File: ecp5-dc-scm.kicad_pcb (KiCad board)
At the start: 6 copper layers, 90 x 120.4 mm, 238 parts, among them IC1 TPS54561, J1 WE-RJ45_7499111121A, J10 61300611121, J11 S2B-PH-K-S_LF__SN_, J2 1-2199230-6, J3 543630489, J4 M20-7830642, J5 SFF-TA-1002-4C+, J6 2X05, Q1 IRLML6402TRPBF, Q10 2N7002, Q11 2N7002, Q12 2N7002, Q2 IRLML6402TRPBF, Q3 IRLML6402TRPBF, Q4 IRLML6402TRPBF, Q5 IRLML6402TRPBF, Q6 2N7002, Q7 2N7002, Q8 2N7002, Q9 2N7002, U1 KSZ9031RNXCA, U10 LM21212-2, U11 SN74LVC1G11DBVR, U14 TPS62823DLCT, U15 TPS62823DLCT, U16 TPS62823DLCT, U17 TPS62823DLCT, U18 ECP5UM5G_85_CABGA756, U2 W25Q32JVSSIQ_TR, U3 W25Q32JVSSIQ_TR, U4 W25Q32JVSSIQ_TR, U5 W25Q32JVSSIQ_TR, U6 NVT2008DQ,115, U7 AS4C256M16D3, U8 TPS51200DRC, Y1 ABM8G-25.000MHZ-18-D2Y-T

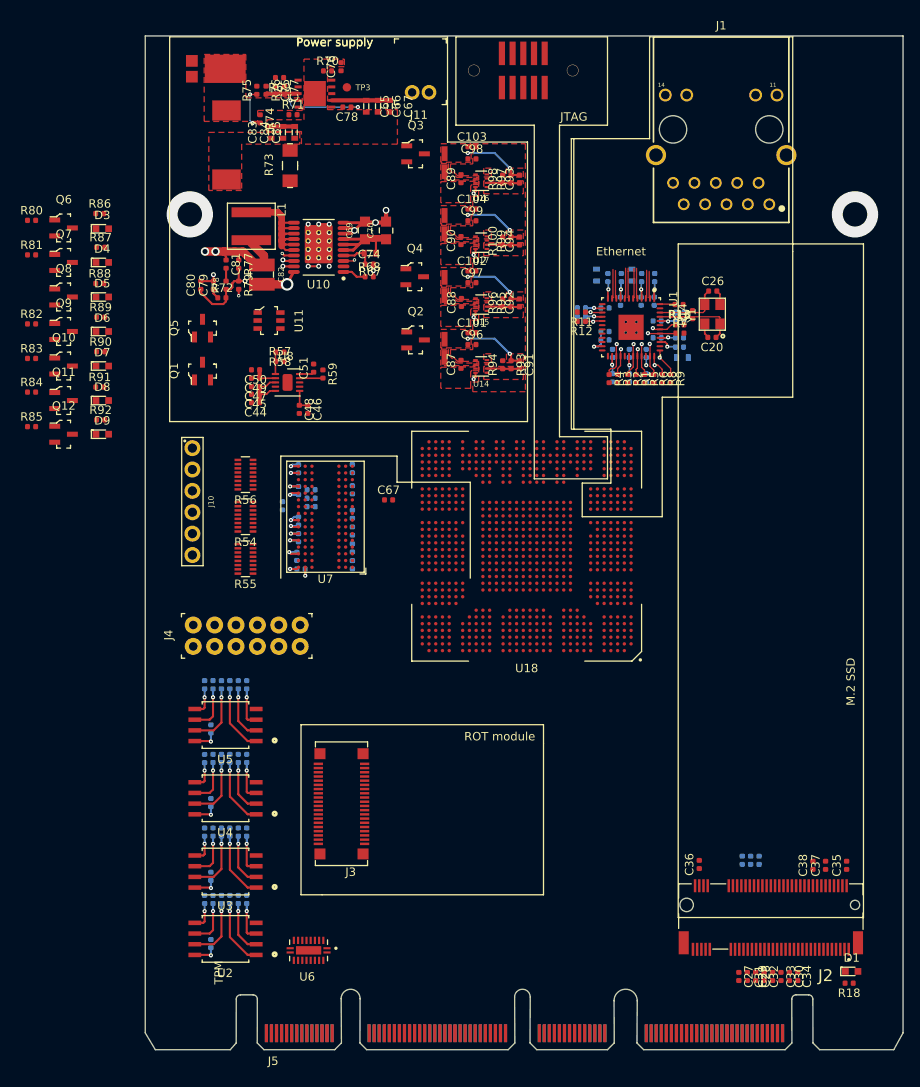
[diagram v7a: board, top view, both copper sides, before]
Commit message: Add component placement-power supply
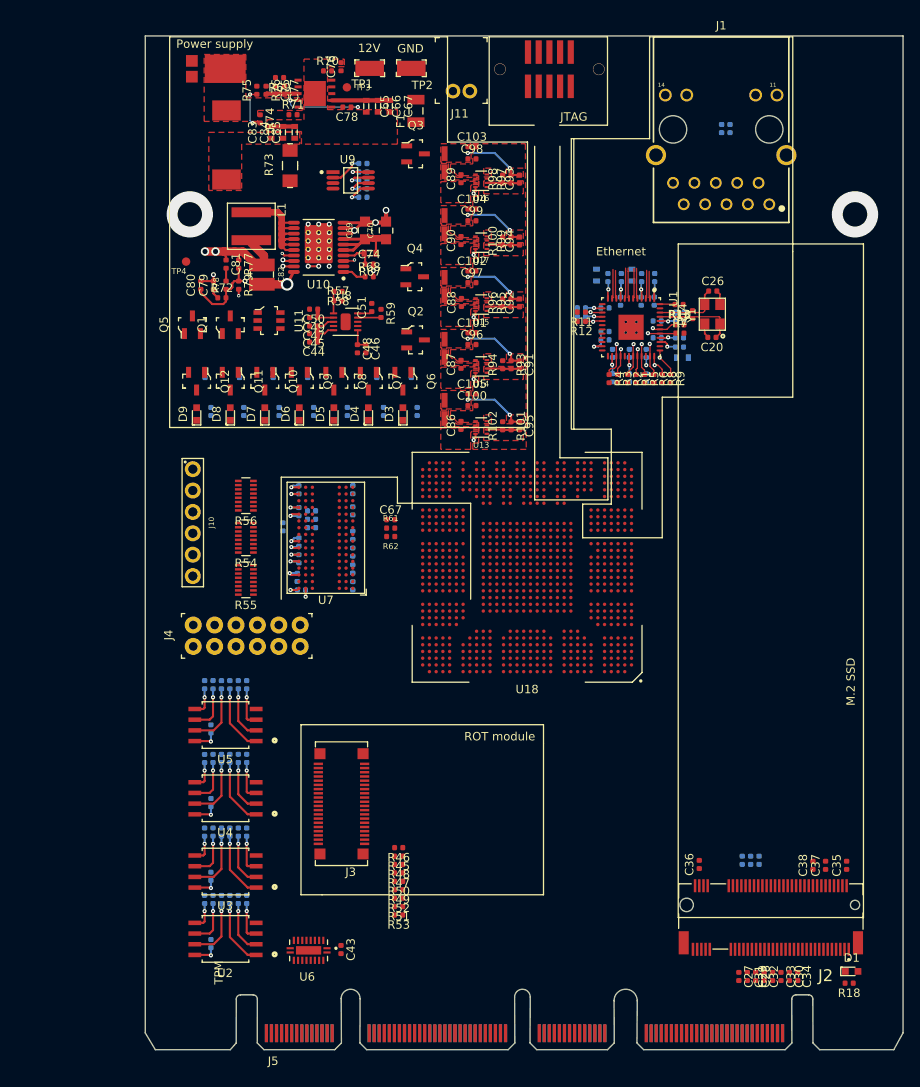
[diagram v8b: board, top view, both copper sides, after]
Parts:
- added C100: C_10u_0402, ecp5-dc-scm-footprints:0402-cap, F.Cu at (98.9, 102.8)
- added C105: C_10u_0402, ecp5-dc-scm-footprints:0402-cap, F.Cu at (98.9, 101.4)
- added C43: C_100n_0402, ecp5-dc-scm-footprints:0402-cap, F.Cu at (83.3, 167.4)
- added C68: C_10n_0402, ecp5-dc-scm-footprints:0402-cap, B.Cu at (86.0, 78.0)
- added C86: C_10u_0402, ecp5-dc-scm-footprints:0402-cap, F.Cu at (97.6, 105.2)
- added C95: C_120p_0402, ecp5-dc-scm-footprints:0402-res, F.Cu at (104.5, 105.2)
- added F1: 0466003.NR, antmicro-footprints:1206-Fuse-Littelfuse-0466-0-0-MFG, F.Cu at (92.2, 67.8)
- added L7: IHLP1212AEERR47M11, antmicro-footprints:IHLP-1212AE, F.Cu at (95.7, 103.2)
- added R101: R_453k_0402, ecp5-dc-scm-footprints:0402-res, F.Cu at (103.5, 105.2)
- added R102: R_100k_0402, ecp5-dc-scm-footprints:0402-res, F.Cu at (102.5, 105.2)
- added R15: R_1k_0402, ecp5-dc-scm-footprints:0402-res, B.Cu at (129.6, 69.9)
- added R16: R_1k_0402, ecp5-dc-scm-footprints:0402-res, B.Cu at (128.6, 69.9)
- added R45: R_357k_0402, ecp5-dc-scm-footprints:0402-res, F.Cu at (90.2, 156.3)
- added R46: R_357k_0402, ecp5-dc-scm-footprints:0402-res, F.Cu at (90.2, 155.3)
- added R47: R_357k_0402, ecp5-dc-scm-footprints:0402-res, F.Cu at (90.2, 158.3)
- added R48: R_357k_0402, ecp5-dc-scm-footprints:0402-res, F.Cu at (90.2, 157.3)
- added R49: R_357k_0402, ecp5-dc-scm-footprints:0402-res, F.Cu at (90.2, 160.3)
- added R50: R_357k_0402, ecp5-dc-scm-footprints:0402-res, F.Cu at (90.2, 159.3)
- added R51: R_357k_0402, ecp5-dc-scm-footprints:0402-res, F.Cu at (90.2, 162.3)
- added R52: R_357k_0402, ecp5-dc-scm-footprints:0402-res, F.Cu at (90.2, 161.3)
- added R53: R_200k_0402, ecp5-dc-scm-footprints:0402-res, F.Cu at (90.2, 163.3)
- added R61: R_51R_0402, antmicro-footprints:0402-res, F.Cu at (89.2, 117.3)
- added R62: R_51R_0402, antmicro-footprints:0402-res, F.Cu at (89.2, 118.3)
- added R63: R_1k1_0402, antmicro-footprints:0402-res, B.Cu at (86.0, 74.0)
- added R64: R_1k_0402, ecp5-dc-scm-footprints:0402-res, B.Cu at (86.0, 75.0)
- added R65: R_1k_0402, ecp5-dc-scm-footprints:0402-res, B.Cu at (86.0, 76.0)
- added R66: R_1k_0402, ecp5-dc-scm-footprints:0402-res, B.Cu at (86.0, 77.0)
- added TP1: RCW-0C, antmicro-footprints:PROBE_PAD_1206, F.Cu at (86.8, 62.8)
- added TP2: RCW-0C, antmicro-footprints:PROBE_PAD_1206, F.Cu at (91.7, 62.8)
- added TP4: TP_SMD1MM, ecp5-dc-scm-footprints:Testpoint_smd_1mm, F.Cu at (65.0, 85.8)
- added U13: TPS62823DLCT, ecp5-dc-scm-footprints:QFN-8_2x1mm, F.Cu at (100.0, 105.4)
- added U9: LM3881MME_NOPB, ecp5-dc-scm-footprints:VSSOP8-Texas_Instruments-DGK0008A, F.Cu at (84.5, 76.0)
- R80, R81, R82, R83, R84, R85, R86, R87, R88, R89, R90, R91, R92: moved to B.Cu
- moved R80 48.6 mm to (91.7, 99.0), turned to 90 degrees
- moved R86 44.4 mm to (92.4, 103.5), turned to 90 degrees
- moved Q6 44.2 mm to (90.7, 99.9), turned to 270 degrees
- moved R81 43.4 mm to (87.6, 99.0), turned to 90 degrees
- moved D3 41.9 mm to (90.7, 103.8), turned to 90 degrees
- moved Q7 38.8 mm to (86.6, 99.9), turned to 270 degrees
- moved R87 38.8 mm to (88.4, 103.5), turned to 90 degrees
- moved D4 36.4 mm to (86.6, 103.8), turned to 90 degrees
- moved Q8 33.6 mm to (82.5, 99.9), turned to 270 degrees
- moved R82 33.3 mm to (79.4, 99.0), turned to 90 degrees
- moved R88 33.1 mm to (84.1, 103.5), turned to 90 degrees
- moved D5 30.8 mm to (82.5, 103.8), turned to 90 degrees
- moved R83 28.8 mm to (75.3, 99.0), turned to 90 degrees
- moved Q9 28.6 mm to (78.4, 99.9), turned to 270 degrees
- moved R89 27.7 mm to (80.1, 103.5), turned to 90 degrees
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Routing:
- net VCC2V5: track 0.00 -> 7.62 mm, vias 0 -> 2
- net /Power supply/PWR_EN: track 0.00 -> 3.97 mm, vias 0 -> 1
- net Net-(C95-Pad2): track 0.00 -> 3.89 mm
- net Net-(C68-Pad1): track 0.00 -> 3.19 mm, vias 0 -> 1
- net /Power supply/VCCIO_EN: track 0.00 -> 2.95 mm, vias 0 -> 1
- net /Power supply/VCCAUX_EN: track 0.00 -> 2.90 mm, vias 0 -> 1
- net /Power supply/VCCINT_EN: track 0.00 -> 2.58 mm, vias 0 -> 1
- net /Power supply/2V5_PG: track 0.00 -> 0.84 mm, vias 0 -> 1
- added copper zone on F.Cu, net Net-(L7-Pad1)
- added copper zone on F.Cu, net VCC2V5
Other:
- board text added: "12V"
- board text added: "GND"
